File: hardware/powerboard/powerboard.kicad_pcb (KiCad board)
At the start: 4 copper layers, 81.2 x 50.7 mm, 64 parts, among them J1 USB_B_Micro, J2 Boot, J3 Power, J4 SPI_0, J5 Debug, J6 SPI_1, J7 I2C_0, J8 I2C_1, J9 UART_0, SW1 Oct_Up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

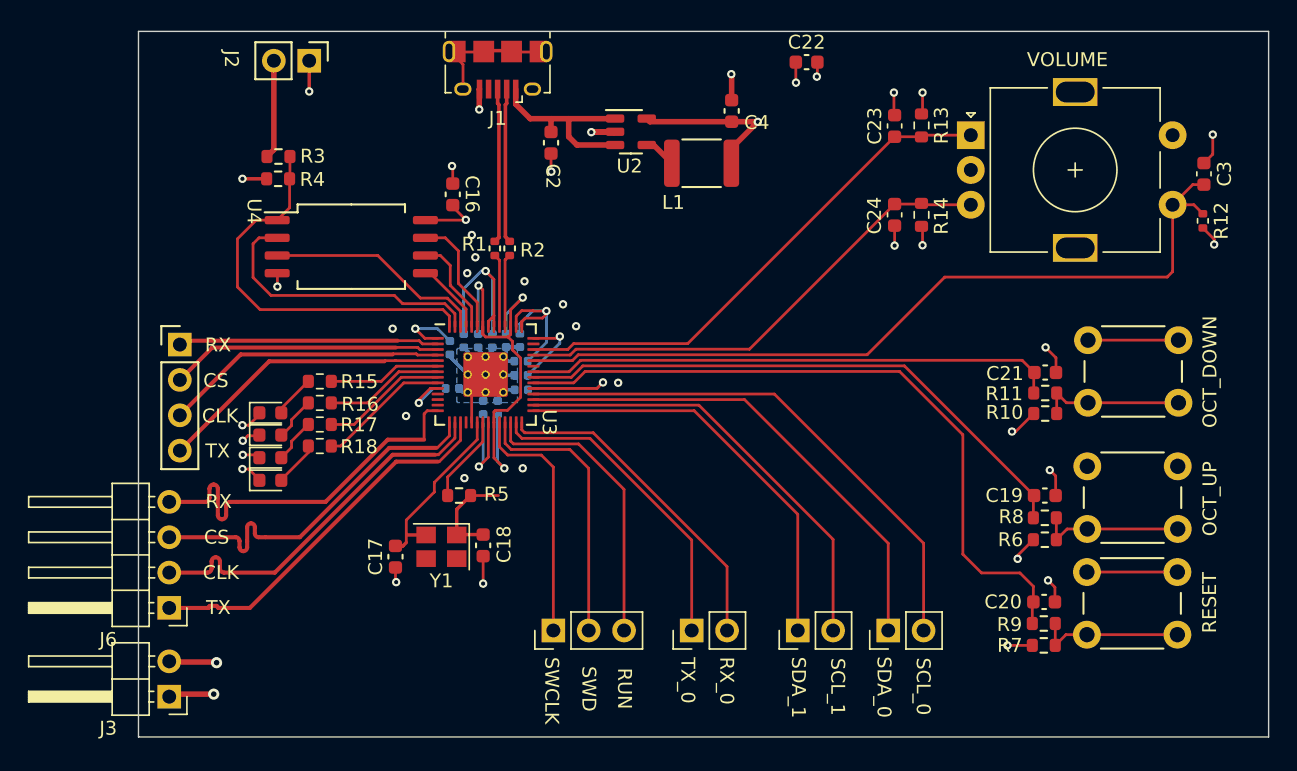
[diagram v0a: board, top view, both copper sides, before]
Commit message: Powerboard Renovations (Stage 1 of Finalization)
Expand SPI 0 Header to match Display Header
Confirm footprints for passives
Power Circuit reorganized for short return paths
Reset button now toggles RUN pin, does not connect to GPIO
GPIO 10 connected to DISPLAY_RESET pin
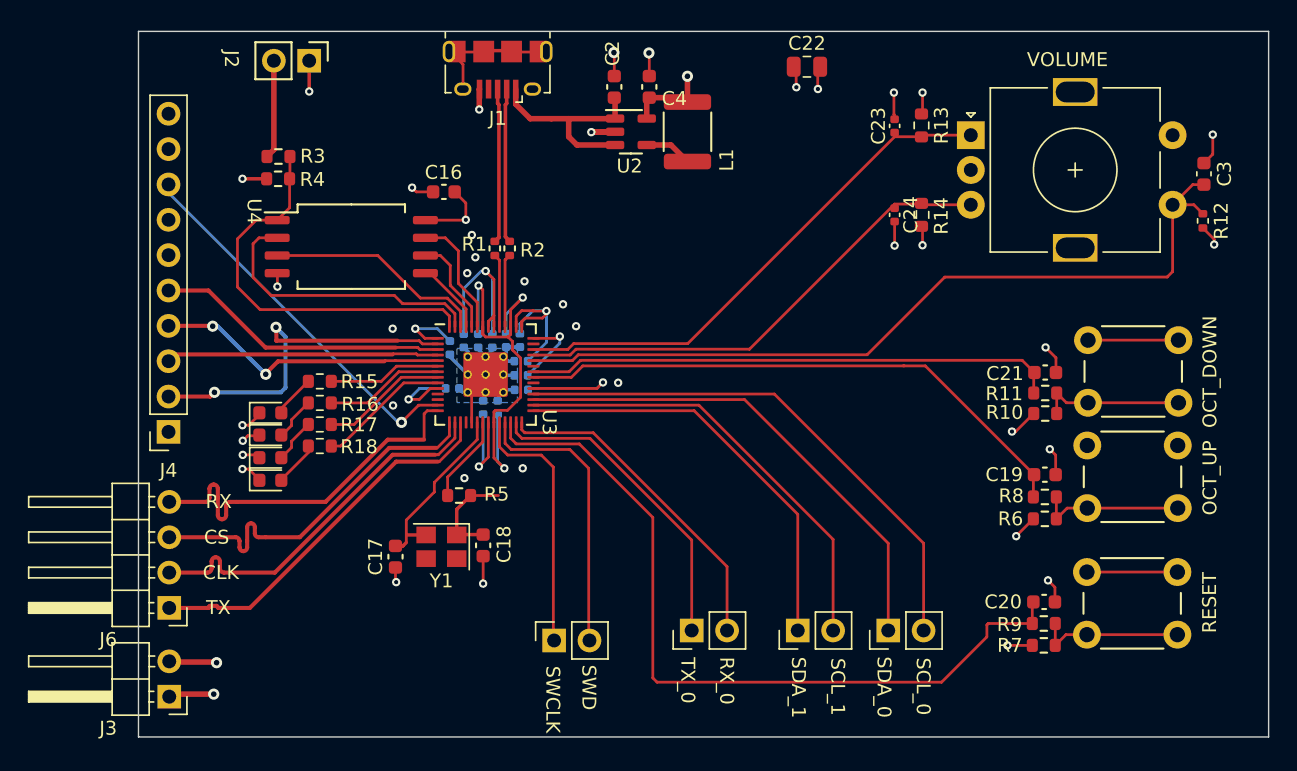
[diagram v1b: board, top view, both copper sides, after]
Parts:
- C16: value 100n -> 100nF
- C22: footprint Capacitor_SMD:C_0603_1608Metric -> Capacitor_SMD:C_0805_2012Metric
- C23, C24: footprint Capacitor_SMD:C_0603_1608Metric -> Capacitor_SMD:C_0402_1005Metric
- J4: value SPI_0 -> Display; footprint Connector_PinHeader_2.54mm:PinHeader_1x04_P2.54mm_Vertical -> Connector_PinSocket_2.54mm:PinSocket_1x10_P2.54mm_Vertical
- J5: footprint Connector_PinHeader_2.54mm:PinHeader_1x03_P2.54mm_Vertical -> Connector_PinSocket_2.54mm:PinSocket_1x02_P2.54mm_Vertical
- R4: value DNF -> 10k
- moved J4 6.33 mm to (52.9, 44.0), turned to 180 degrees
- moved C4 6.17 mm to (87.5, 19.2)
- moved C2 6.06 mm to (85.0, 19.2), turned to 90 degrees
- moved L1 2.48 mm to (90.2, 22.4), turned to 90 degrees
- moved C19 1.50 mm to (115.9, 47.0)
- moved R8 1.50 mm to (115.9, 48.6)
- moved SW1 1.50 mm to (118.9, 44.9)
- moved R6 1.50 mm to (115.9, 50.2)
- moved J5 0.72 mm to (80.6, 59.0)
- moved C16 0.66 mm to (72.7, 26.7), turned to 180 degrees
- moved C22 0.33 mm to (98.8, 17.7)
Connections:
- J4 pad 1: RX -> +3.3V
- J4 pad 2: CS -> RX
- U3 pad 13: unconnected-(U3-Pad13) -> DISPLAY_RESET
- U3 pad 26: /RUN -> RESET
- U3 pad 34: RESET -> unconnected-(U3-Pad34)
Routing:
- net DISPLAY_RESET: track 0.00 -> 27.3 mm, vias 0 -> 1
- net /RUN: track 21.1 -> 0.00 mm
- net RX: track 18.7 -> 26.0 mm, vias 0 -> 2
- net RESET: track 50.4 -> 56.5 mm
- net +3.3V: track 93.2 -> 89.6 mm
- net CS: track 19.6 -> 21.1 mm
- net GND: track 71.4 -> 72.5 mm
- net Net-(L1-Pad1): track 2.35 -> 3.42 mm
- net SCLK: track 20.4 -> 19.6 mm
- net Net-(C2-Pad1): track 14.5 -> 15.1 mm
- net Oct_Up: track 41.8 -> 41.3 mm
- net TX: vias 0 -> 2
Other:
- board text removed: "RUN"

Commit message: Powerboard Finalization
Crystal Footprint and layout changed to match new crystal
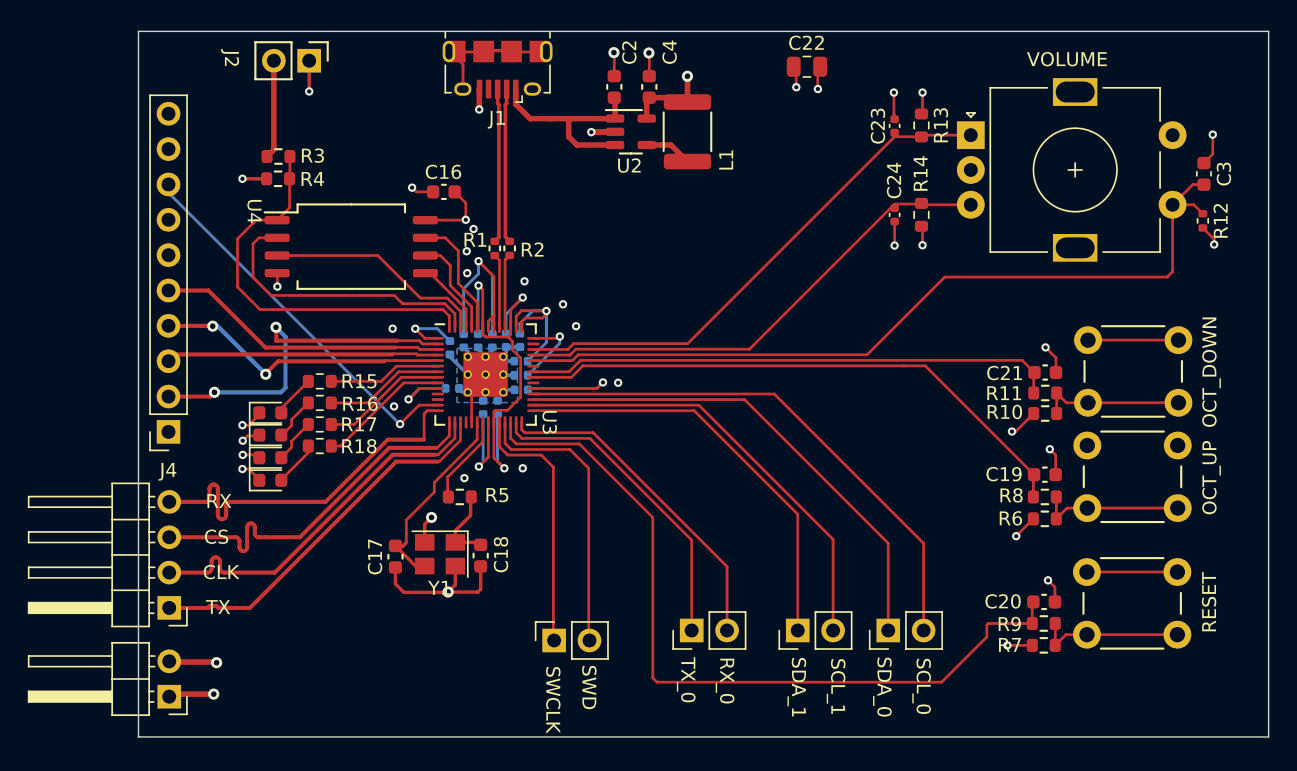
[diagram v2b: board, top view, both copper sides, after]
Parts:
- Y1: value 3N12000G33YC -> Crystal_GND24
- moved C18 0.76 mm to (75.4, 52.9)
- moved Y1 0.54 mm to (72.4, 52.8)
- moved R5 0.11 mm to (73.9, 48.6)
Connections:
- Y1 pad 2: /XIN -> GND
- Y1 pad 3: (no net) -> /XIN
- Y1 pad 4: (no net) -> GND
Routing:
- net GND: track 72.5 -> 82.8 mm
- net +3.3V: track 89.6 -> 91.6 mm
- net Net-(C18-Pad2): track 7.16 -> 5.71 mm
- net /XIN: track 13.0 -> 14.3 mm

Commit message: Powerboard review with sheaff
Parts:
- removed J9: UART_0, Connector_PinHeader_2.54mm:PinHeader_1x02_P2.54mm_Vertical
- added J10: 5V, Connector_PinHeader_2.54mm:PinHeader_1x02_P2.54mm_Vertical, F.Cu at (80.2, 22.8)
- added J11: 3V3, Connector_PinHeader_2.54mm:PinHeader_1x02_P2.54mm_Vertical, F.Cu at (94.5, 20.0)
- C17, C18: value 20p -> 30p
- J7: value I2C_0 -> UART_0; footprint Connector_PinHeader_2.54mm:PinHeader_1x02_P2.54mm_Vertical -> Connector_PinSocket_2.54mm:PinSocket_1x03_P2.54mm_Vertical
- J8: value I2C_1 -> I2C_0; footprint Connector_PinHeader_2.54mm:PinHeader_1x02_P2.54mm_Vertical -> Connector_PinSocket_2.54mm:PinSocket_1x04_P2.54mm_Vertical
- moved J7 16.7 mm to (88.0, 58.8)
- moved J8 0.49 mm to (98.6, 58.2)
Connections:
- C2 pad 1: Net-(C2-Pad1) -> Net-(J10-Pad2)
- C4 pad 1: +3.3V -> Net-(C4-Pad1)
- J1 pad 1: Net-(C2-Pad1) -> Net-(J1-Pad1)
- J7 pad 1: SDA_0 -> GND
- J7 pad 2: SCL_0 -> UART_TX_0
- J8 pad 1: SDA_1 -> SDA_0
- J8 pad 2: SCL_1 -> SCL_0
- L1 pad 2: +3.3V -> Net-(C4-Pad1)
- U2 pad 1: Net-(C2-Pad1) -> Net-(J10-Pad2)
- U2 pad 3: Net-(C2-Pad1) -> Net-(J10-Pad2)
- U2 pad 5: +3.3V -> Net-(C4-Pad1)
- U3 pad 29: SDA_1 -> unconnected-(U3-Pad29)
- U3 pad 30: SCL_1 -> unconnected-(U3-Pad30)
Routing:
- net SCL_1: track 32.1 -> 0.00 mm
- net SDA_1: track 30.4 -> 0.00 mm
- net Net-(C2-Pad1): track 15.1 -> 0.00 mm
- net Net-(J10-Pad2): track 0.00 -> 13.4 mm
- net Net-(C4-Pad1): track 0.00 -> 8.85 mm
- net DISPLAY_RESET: track 27.4 -> 33.9 mm
- net +3.3V: track 91.6 -> 85.3 mm, vias 18 -> 17
- net Net-(J1-Pad1): track 0.00 -> 4.44 mm
- net SCL_0: track 38.7 -> 35.2 mm
- net SDA_0: track 36.0 -> 33.6 mm
- net RESET: track 56.5 -> 57.3 mm
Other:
- board text added: "3.3V"
- board text removed: "SCL_1"
- board text removed: "SDA_1"

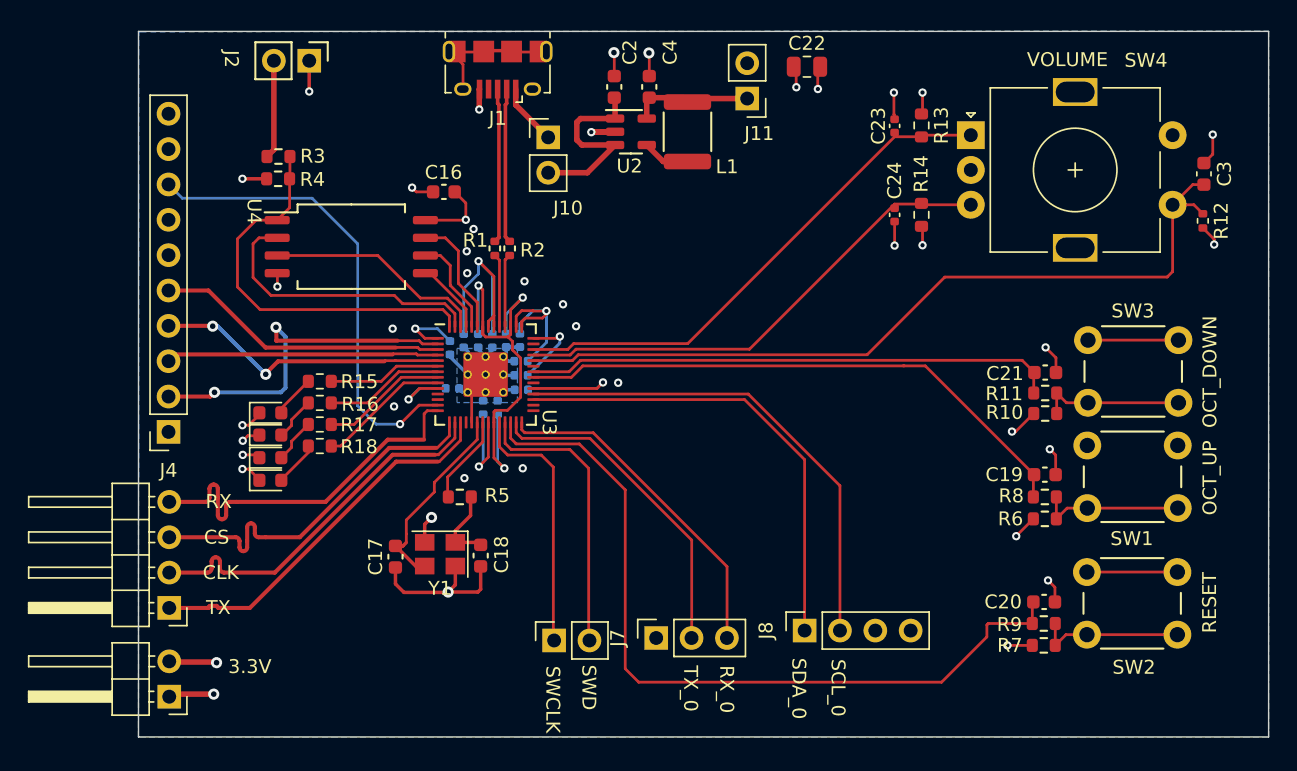
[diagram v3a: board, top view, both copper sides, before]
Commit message: Powerboard PCB Revisions
Expanded I2C Headers to include 3.3V and GND
Expanded UART Header to include GND
Expanded SWD Header to include GND
Added Silkscreen for All(?) Parts
Added GND Fill on Back Layer
Added header for 3.3V and 5V Current Measurements
Powerboard has all parts picked out and ready to order on JLC
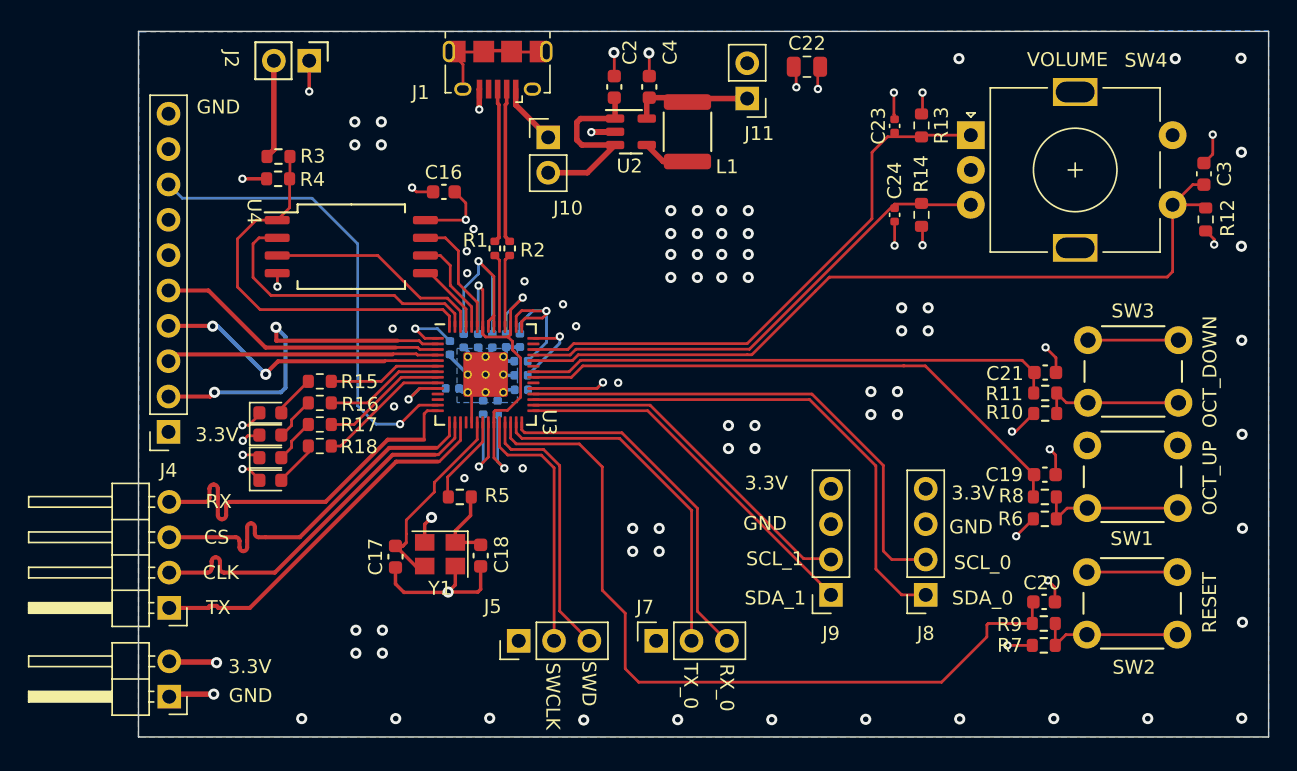
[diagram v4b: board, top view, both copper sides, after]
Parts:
- added J9: I2C_1, Connector_PinSocket_2.54mm:PinSocket_1x04_P2.54mm_Vertical, F.Cu at (100.5, 55.7)
- J10: value 5V -> 5V Header
- J11: value 3V3 -> 3V3 Header
- J5: footprint Connector_PinSocket_2.54mm:PinSocket_1x02_P2.54mm_Vertical -> Connector_PinHeader_2.54mm:PinHeader_1x03_P2.54mm_Vertical
- R12: footprint Resistor_SMD:R_0402_1005Metric -> Resistor_SMD:R_0603_1608Metric
- moved J8 9.07 mm to (107.3, 55.7), turned to 180 degrees
- moved J5 2.55 mm to (78.1, 59.0)
- moved R12 0.23 mm to (127.5, 28.7)
- moved J7 0.20 mm to (88.0, 59.0)
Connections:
- J5 pad 1: /SWCLK -> GND
- J5 pad 2: /SWD -> /SWCLK
- U3 pad 29: unconnected-(U3-Pad29) -> SDA_1
- U3 pad 30: unconnected-(U3-Pad30) -> SCL_1
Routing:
- net SDA_1: track 0.00 -> 26.8 mm
- net SCL_1: track 0.00 -> 26.0 mm
- net SDA_0: track 33.6 -> 38.3 mm
- net A: track 37.8 -> 40.6 mm
- net UART_RX_0: track 23.9 -> 25.9 mm
- net SCL_0: track 35.2 -> 36.7 mm
- net UART_TX_0: track 23.0 -> 24.3 mm
- net GND: vias 32 -> 92
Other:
- board text added: "GND"
- board text added: "SCL_1"
- board text added: "SDA_1"

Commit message: more adjustments on powerboard
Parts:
- moved C17 2.92 mm to (70.2, 50.2), turned to 180 degrees
- moved C18 2.80 mm to (74.4, 50.2), turned to 0 degrees
- moved R5 0.20 mm to (73.7, 48.6)
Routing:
- net GND: track 82.8 -> 75.7 mm
- net Net-(C18-Pad2): track 5.71 -> 4.29 mm

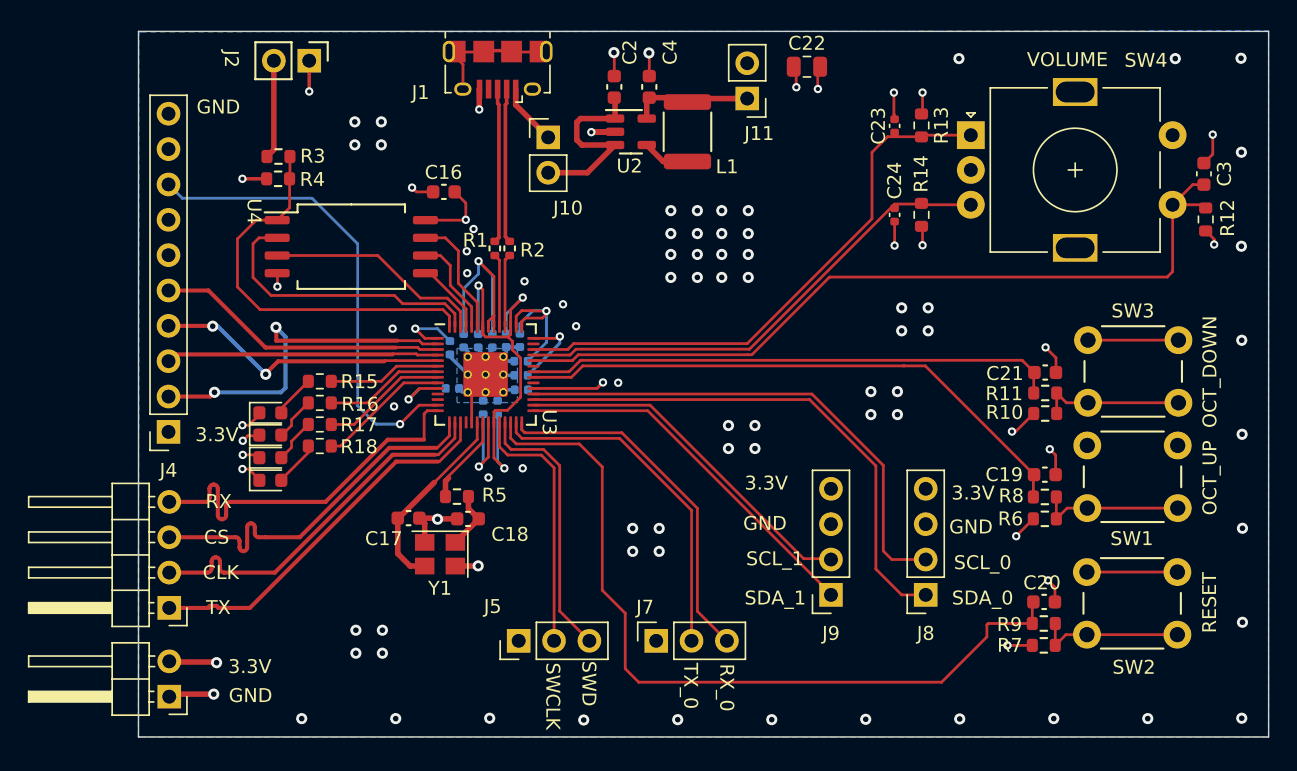
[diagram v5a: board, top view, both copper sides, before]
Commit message: JLC Capabilities Double Checked
Confirmed JLC Capabilities with Design Rules
CHECK SILKSCREEN RULES
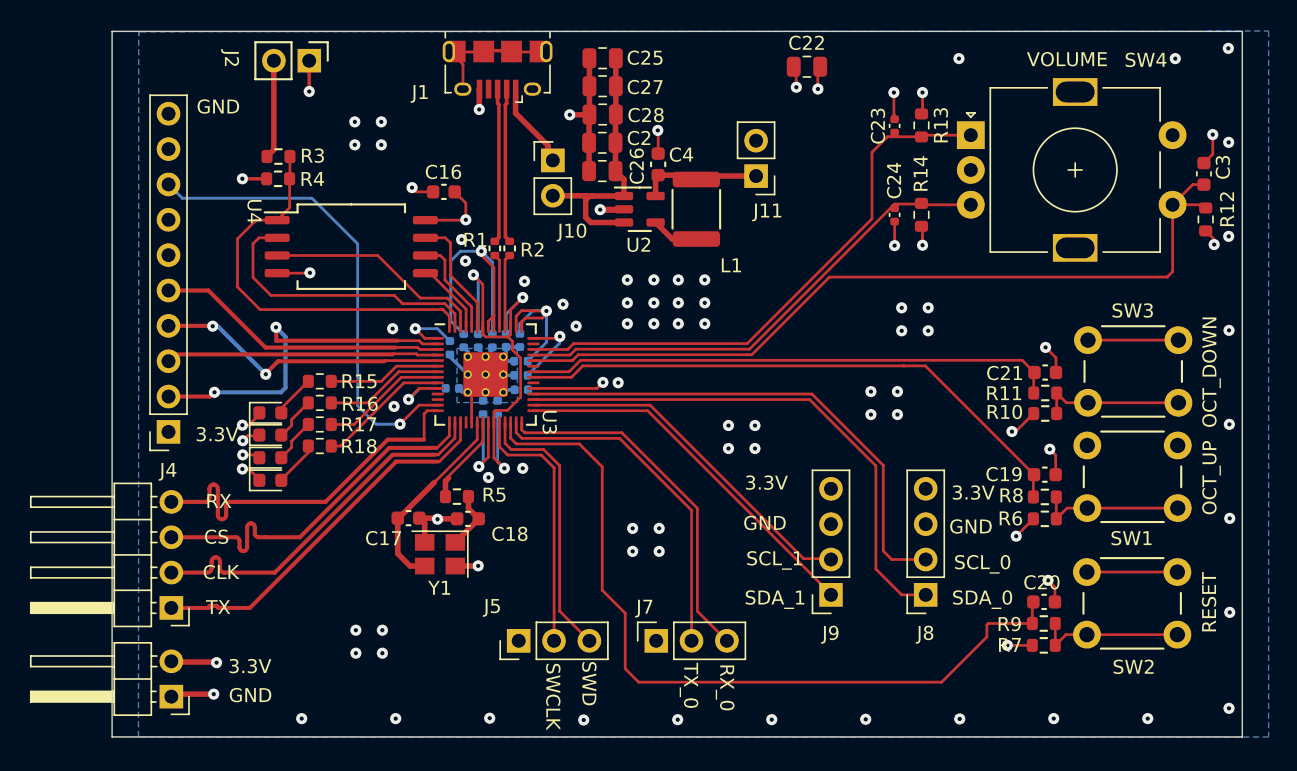
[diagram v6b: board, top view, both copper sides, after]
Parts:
- added C25: 1uF, Capacitor_SMD:C_0805_2012Metric, F.Cu at (84.1, 17.1)
- added C26: 1uF, Capacitor_SMD:C_0805_2012Metric, F.Cu at (84.1, 25.2)
- added C27: 1uF, Capacitor_SMD:C_0805_2012Metric, F.Cu at (84.1, 19.1)
- added C28: 1uF, Capacitor_SMD:C_0805_2012Metric, F.Cu at (84.1, 21.2)
- C2: value 4.7uF -> 1uF; footprint Capacitor_SMD:C_0603_1608Metric -> Capacitor_SMD:C_0805_2012Metric
- J10: value 5V Header -> 5V
- J11: value 3V3 Header -> 3V3
- moved L1 5.60 mm to (90.9, 28.0)
- moved U2 5.60 mm to (86.8, 28.0)
- moved C4 5.60 mm to (88.1, 24.7)
- moved J11 5.60 mm to (95.2, 25.6)
- moved C2 4.11 mm to (84.1, 23.2), turned to 180 degrees
- moved J10 1.69 mm to (80.5, 24.5)
- moved J3 0.15 mm to (53.1, 63.0)
- moved J6 0.15 mm to (53.1, 56.6)
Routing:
- net GND: track 75.7 -> 84.9 mm, vias 92 -> 87
- net Net-(J10-Pad2): track 13.4 -> 19.3 mm
- net +3.3V: track 85.3 -> 89.0 mm
- net +1V1: track 31.4 -> 33.2 mm
- net Net-(J1-Pad1): track 4.44 -> 5.64 mm
